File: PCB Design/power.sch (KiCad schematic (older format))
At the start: 18 parts, among them P1 CONN_01X03, P2 CONN_01X02, U1 3.3VREG

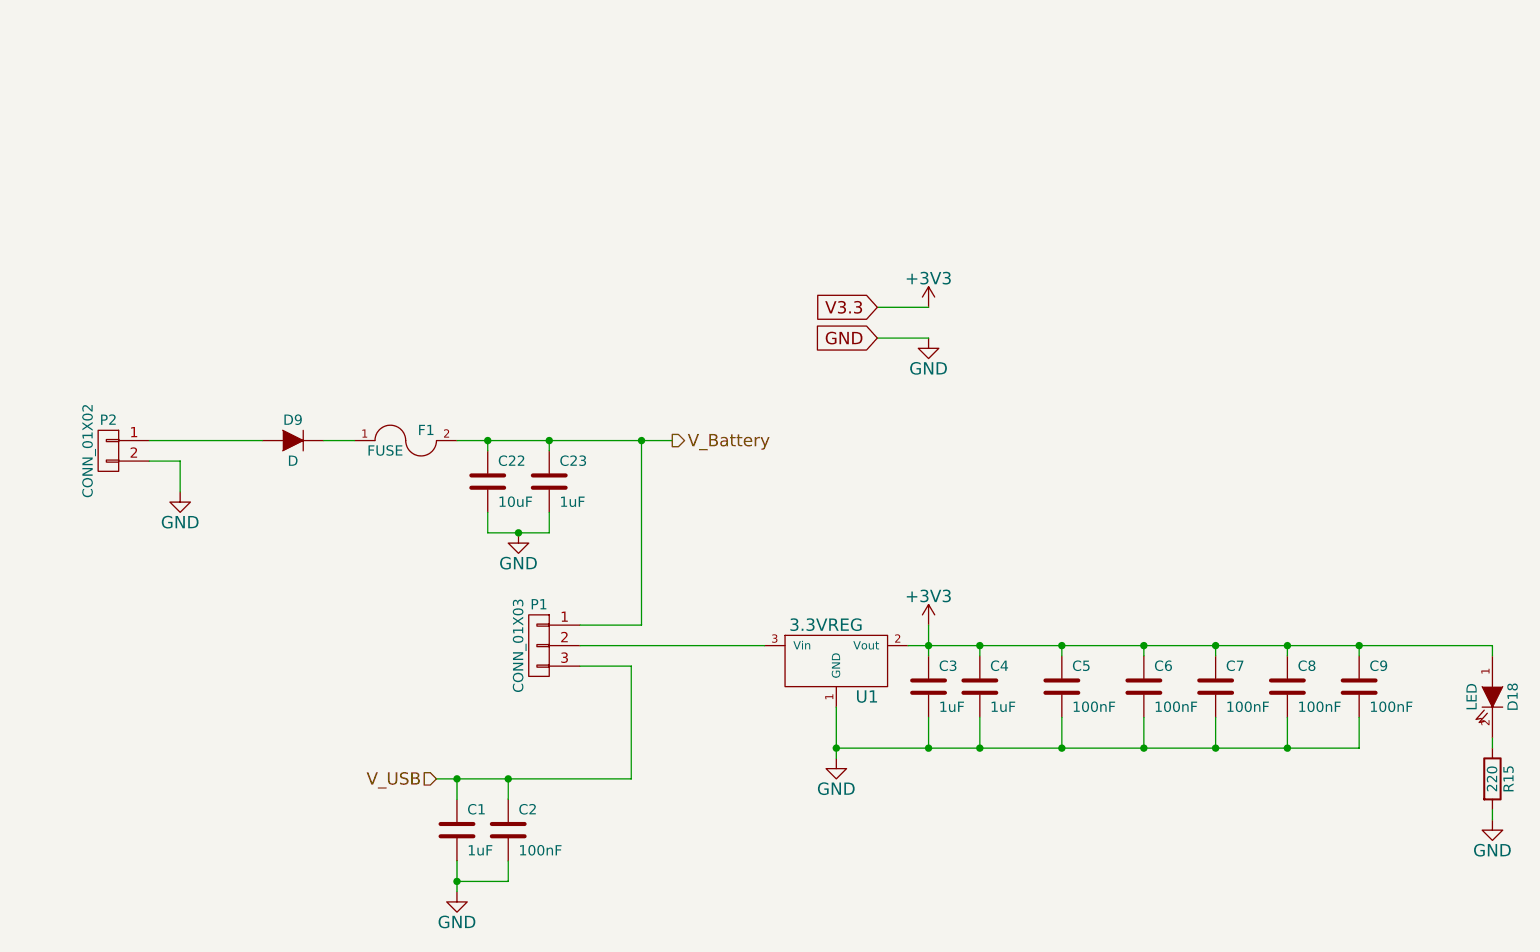
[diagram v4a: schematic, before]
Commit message: Finished the footprint allocation, started on the PCB layout.-s
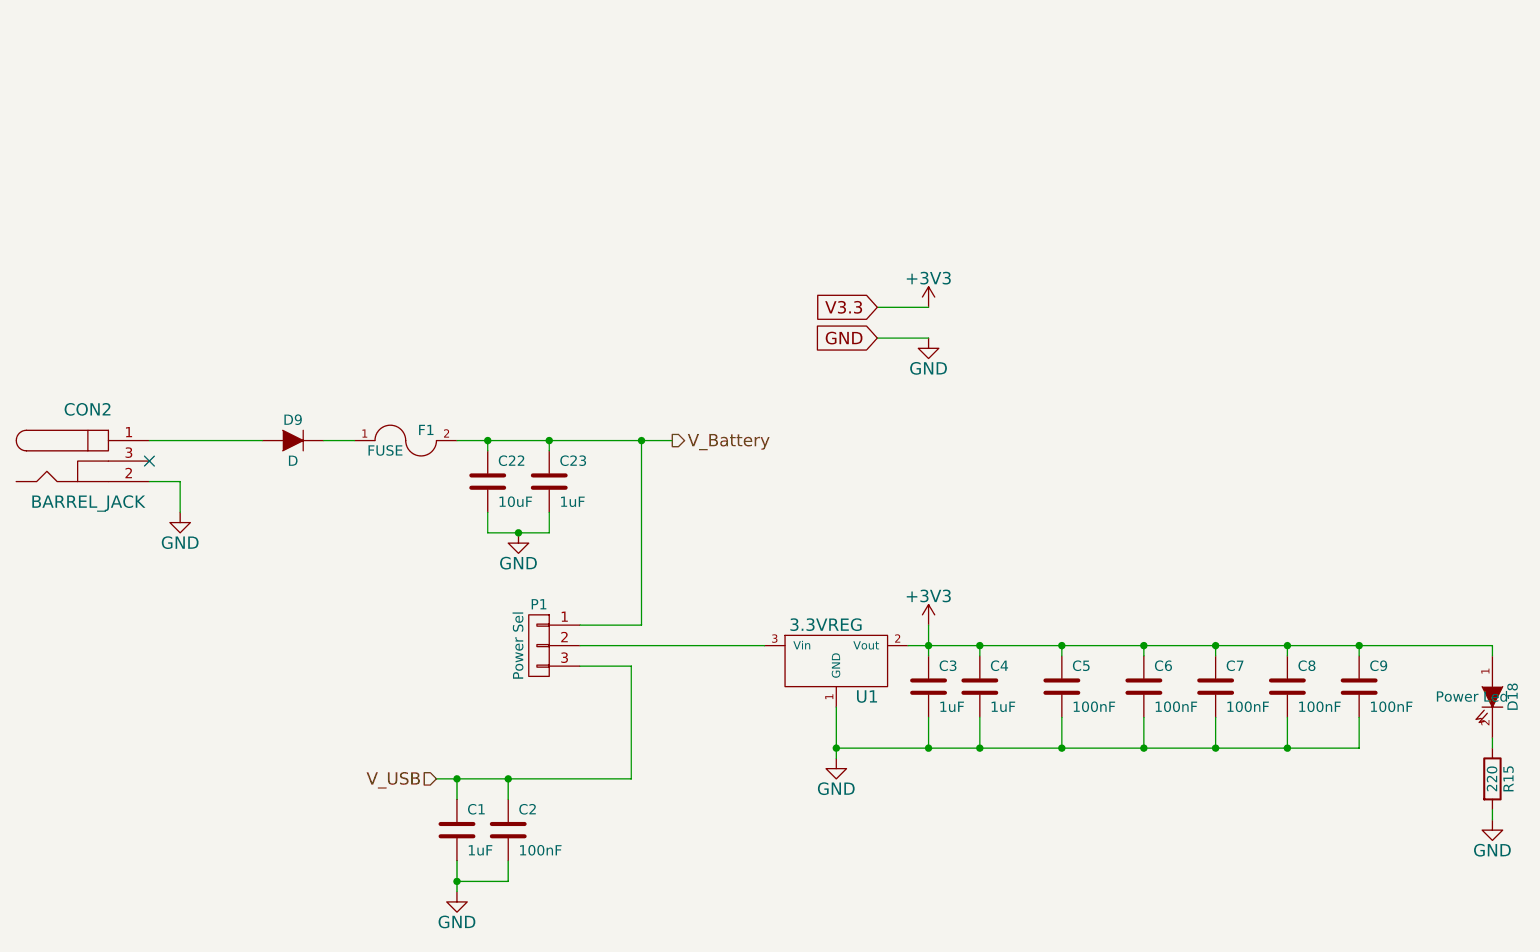
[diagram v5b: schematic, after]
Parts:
- removed P2: CONN_01X02, symbol CONN_01X02
- added CON2: BARREL_JACK, Connect:BARREL_JACK, symbol BARREL_JACK
- D18: value LED -> Power Led; footprint (none) -> LEDs:LED-1206
- D9: footprint (none) -> Diodes_SMD:Diode-SMC_Handsoldering
- F1: footprint (none) -> Resistors_SMD:R_1206_HandSoldering
- P1: value CONN_01X03 -> Power Sel
- U1: footprint (none) -> SMD_Packages:SOT-223
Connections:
- net GND: now also CON2.2
- net at D9.1 (A): now also CON2.1
- no-connect marks 0 -> 1
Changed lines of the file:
@@
 $EndDescr
 $Comp
-L +3V3 #PWR5
+L +3V3 #PWR01
 U 1 1 551253EA
 P 6600 2250
-F 0 "#PWR5" H 6600 2100 60  0001 C CNN
+F 0 "#PWR01" H 6600 2100 60  0001 C CNN
 F 1 "+3V3" H 6600 2390 60  0000 C CNN
 F 2 "" H 6600 2250 60  0000 C CNN
@@
 $EndComp
 $Comp
-L GND #PWR6
+L GND #PWR02
 U 1 1 551253F0
 P 6600 2400
-F 0 "#PWR6" H 6600 2150 60  0001 C CNN
+F 0 "#PWR02" H 6600 2150 60  0001 C CNN
 F 1 "GND" H 6600 2250 60  0000 C CNN
 F 2 "" H 6600 2400 60  0000 C CNN
@@
 P 4700 3900
 F 0 "P1" H 4700 4100 50  0000 C CNN
-F 1 "CONN_01X03" V 4800 3900 50  0000 C CNN
+F 1 "Power Sel" V 4800 3900 50  0000 C CNN
 F 2 "Pin_Headers:Pin_Header_Straight_1x03" H 4700 3900 60  0001 C CNN
 F 3 "" H 4700 3900 60  0000 C CNN
@@
 F 0 "U1" H 6300 3650 60  0000 C CNN
 F 1 "3.3VREG" H 6100 4000 60  0000 C CNN
-F 2 "" H 6150 3900 60  0001 C CNN
+F 2 "SMD_Packages:SOT-223" H 6150 3900 60  0001 C CNN
 F 3 "" H 6150 3900 60  0000 C CNN
 	1    6150 3900
@@
 $EndComp
 $Comp
-L +3V3 #PWR7
+L +3V3 #PWR03
 U 1 1 551258E1
 P 6600 3800
-F 0 "#PWR7" H 6600 3650 60  0001 C CNN
+F 0 "#PWR03" H 6600 3650 60  0001 C CNN
 F 1 "+3V3" H 6600 3940 60  0000 C CNN
 F 2 "" H 6600 3800 60  0000 C CNN
@@
 	6600 3800 6600 3950
 $Comp
-L GND #PWR4
+L GND #PWR04
 U 1 1 55125915
 P 6150 4450
-F 0 "#PWR4" H 6150 4200 60  0001 C CNN
+F 0 "#PWR04" H 6150 4200 60  0001 C CNN
 F 1 "GND" H 6150 4300 60  0000 C CNN
 F 2 "" H 6150 4450 60  0000 C CNN
@@
 $EndComp
 $Comp
-L GND #PWR2
+L GND #PWR05
 U 1 1 55125A29
 P 4300 5100
-F 0 "#PWR2" H 4300 4850 60  0001 C CNN
+F 0 "#PWR05" H 4300 4850 60  0001 C CNN
 F 1 "GND" H 4300 4950 60  0000 C CNN
 F 2 "" H 4300 5100 60  0000 C CNN
@@
 Connection ~ 8350 3900
 $Comp
-L CONN_01X02 P2
-U 1 1 551263E1
-P 2600 2950
-F 0 "P2" H 2600 3100 50  0000 C CNN
-F 1 "CONN_01X02" V 2700 2950 50  0000 C CNN
-F 2 "" H 2600 2950 60  0001 C CNN
-F 3 "" H 2600 2950 60  0000 C CNN
-	1    2600 2950
-	-1   0    0    -1
-$EndComp
-$Comp
-L GND #PWR1
+L GND #PWR06
 U 1 1 551264A9
-P 2950 3150
-F 0 "#PWR1" H 2950 2900 60  0001 C CNN
-F 1 "GND" H 2950 3000 60  0000 C CNN
-F 2 "" H 2950 3150 60  0000 C CNN
-F 3 "" H 2950 3150 60  0000 C CNN
-	1    2950 3150
-	1    0    0    -1
-$EndComp
-Wire Wire Line
-	2800 3000 2950 3000
-Wire Wire Line
-	2950 3000 2950 3150
+P 2950 3250
+F 0 "#PWR06" H 2950 3000 60  0001 C CNN
+F 1 "GND" H 2950 3100 60  0000 C CNN
+F 2 "" H 2950 3250 60  0000 C CNN
+F 3 "" H 2950 3250 60  0000 C CNN
+	1    2950 3250
+	1    0    0    -1
+$EndComp
+Wire Wire Line
+	2950 3100 2950 3250
 $Comp
 L FUSE F1
@@
 F 0 "F1" H 4150 2950 50  0000 C CNN
 F 1 "FUSE" H 3950 2850 50  0000 C CNN
-F 2 "" H 4050 2900 60  0001 C CNN
+F 2 "Resistors_SMD:R_1206_HandSoldering" H 4050 2900 60  0001 C CNN
 F 3 "" H 4050 2900 60  0000 C CNN
 	1    4050 2900
 	1    0    0    -1
 $EndComp
-Wire Wire Line
-	2800 2900 3350 2900
 Wire Wire Line
 	6850 3900 6850 3950
@@
 Connection ~ 4450 2900
 $Comp
-L GND #PWR3
+L GND #PWR07
 U 1 1 5513CAE7
 P 4600 3350
-F 0 "#PWR3" H 4600 3100 60  0001 C CNN
+F 0 "#PWR07" H 4600 3100 60  0001 C CNN
 F 1 "GND" H 4600 3200 60  0000 C CNN
 F 2 "" H 4600 3350 60  0000 C CNN
@@
 F 0 "D9" H 3500 3000 50  0000 C CNN
 F 1 "D" H 3500 2800 50  0000 C CNN
-F 2 "" H 3500 2900 60  0001 C CNN
+F 2 "Diodes_SMD:Diode-SMC_Handsoldering" H 3500 2900 60  0001 C CNN
 F 3 "" H 3500 2900 60  0000 C CNN
 	1    3500 2900
@@
 P 9350 4150
 F 0 "D18" H 9350 4250 50  0000 C CNN
-F 1 "LED" H 9350 4050 50  0000 C CNN
-F 2 "" H 9350 4150 60  0001 C CNN
+F 1 "Power Led" V 9350 4050 50  0000 C CNN
+F 2 "LEDs:LED-1206" H 9350 4150 60  0001 C CNN
 F 3 "" H 9350 4150 60  0000 C CNN
 	1    9350 4150
@@
 $EndComp
 $Comp
-L GND #PWR8
+L GND #PWR08
 U 1 1 551841D4
 P 9350 4750
-F 0 "#PWR8" H 9350 4500 60  0001 C CNN
+F 0 "#PWR08" H 9350 4500 60  0001 C CNN
 F 1 "GND" H 9350 4600 60  0000 C CNN
 F 2 "" H 9350 4750 60  0000 C CNN
@@
 	9350 3900 9350 3950
 Connection ~ 8700 3900
+$Comp
+L BARREL_JACK CON2
+U 1 1 551A8563
+P 2500 3000
+F 0 "CON2" H 2500 3250 60  0000 C CNN
+F 1 "BARREL_JACK" H 2500 2800 60  0000 C CNN
+F 2 "Connect:BARREL_JACK" H 2500 3000 60  0001 C CNN
+F 3 "" H 2500 3000 60  0000 C CNN
+	1    2500 3000
+	1    0    0    -1
+$EndComp
+Wire Wire Line
+	2800 3100 2950 3100
+Wire Wire Line
+	2800 2900 3350 2900
+NoConn ~ 2800 3000
 $EndSCHEMATC

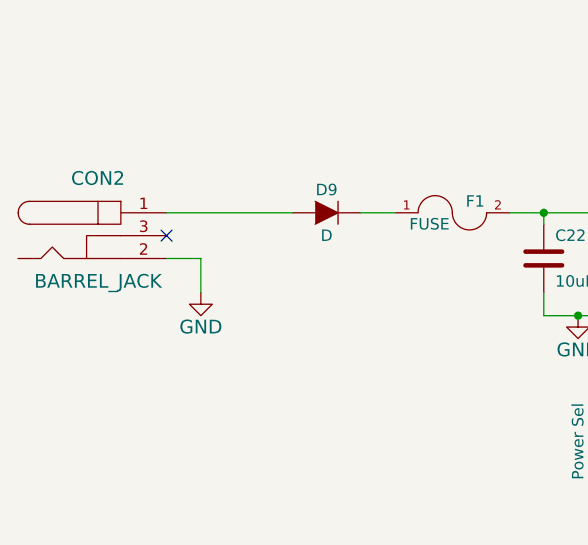
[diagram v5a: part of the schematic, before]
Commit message: Connected 2nd floating ground to ground (updated pdf and .net to reflect this)
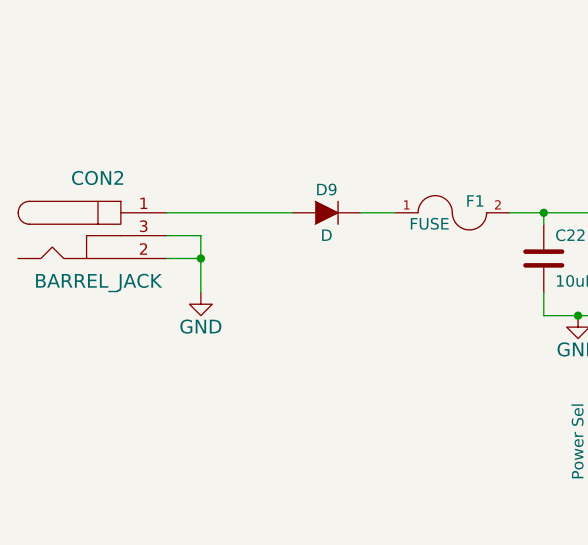
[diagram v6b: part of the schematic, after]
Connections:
- net GND: now also CON2.3
- no-connect marks 1 -> 0
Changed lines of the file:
@@
 $EndComp
 Wire Wire Line
-	2950 3100 2950 3250
+	2950 3000 2950 3250
 $Comp
 L FUSE F1
@@
 	9350 3900 9350 3950
 Connection ~ 8700 3900
+Wire Wire Line
+	2800 3100 2950 3100
+Wire Wire Line
+	2800 2900 3350 2900
 $Comp
 L BARREL_JACK CON2
@@
 $EndComp
 Wire Wire Line
-	2800 3100 2950 3100
-Wire Wire Line
-	2800 2900 3350 2900
-NoConn ~ 2800 3000
+	2800 3000 2950 3000
+Connection ~ 2950 3100
 $EndSCHEMATC
